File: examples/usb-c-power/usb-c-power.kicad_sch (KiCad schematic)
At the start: 10 parts, among them J1 USB4105-GF-A, J2 Fused 5 V OUT

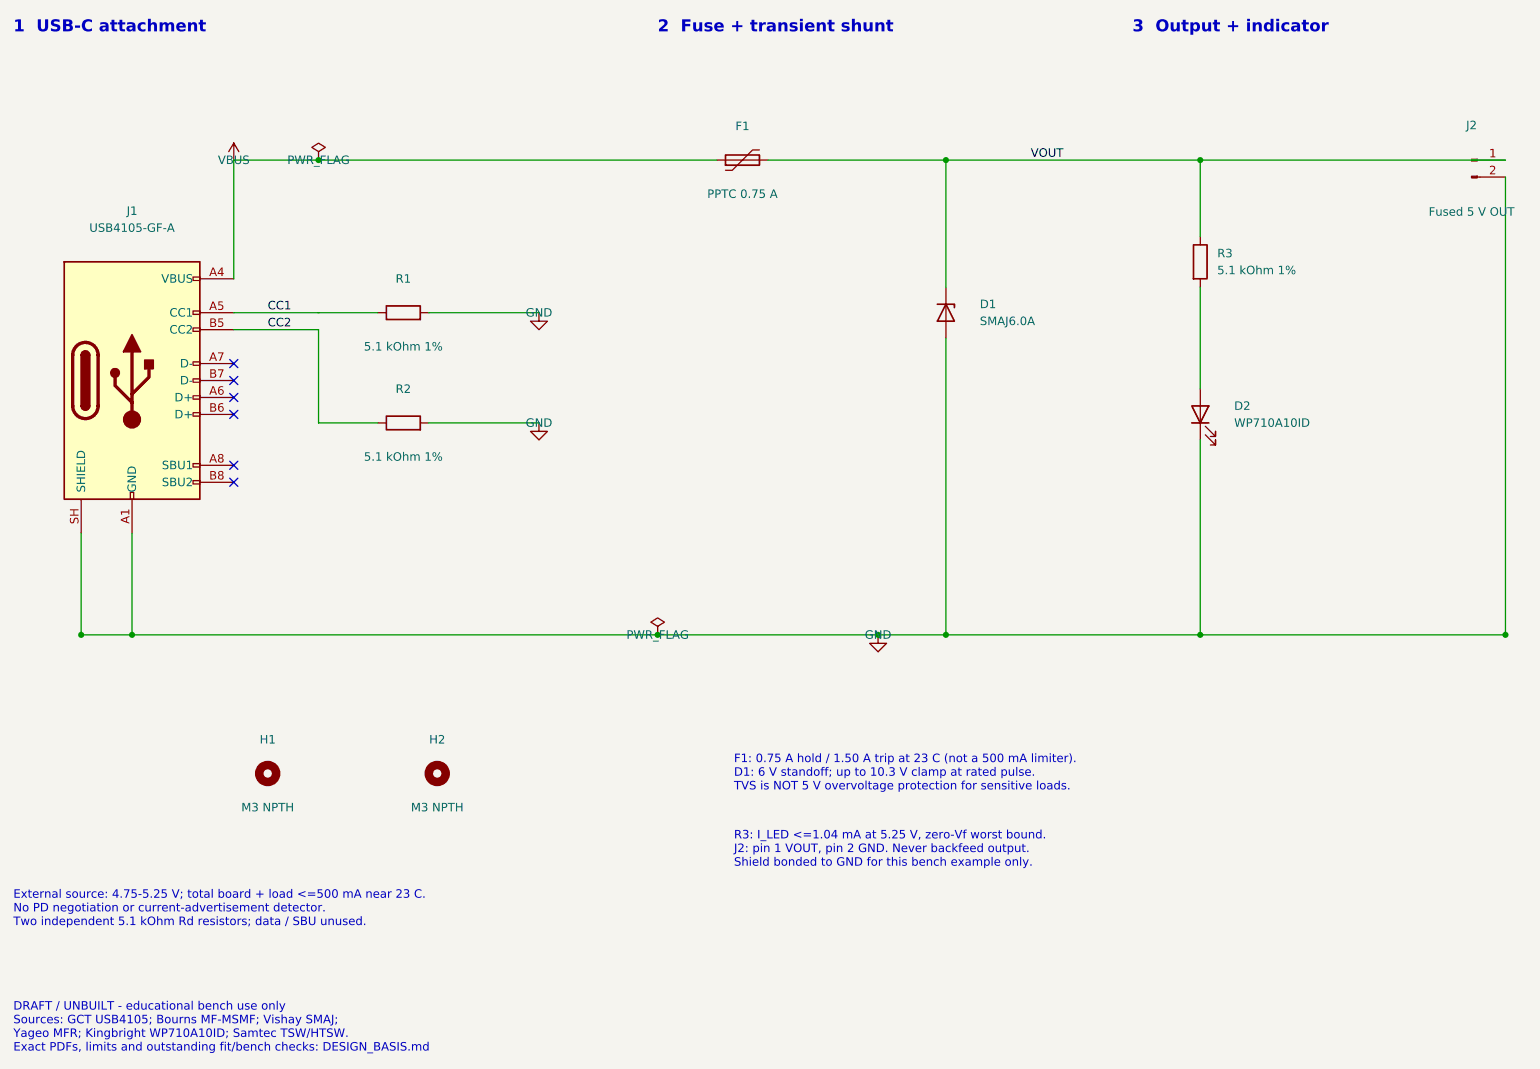
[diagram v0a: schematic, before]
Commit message: Resolve USB-C connector DRC with compatible manufacturer geometry
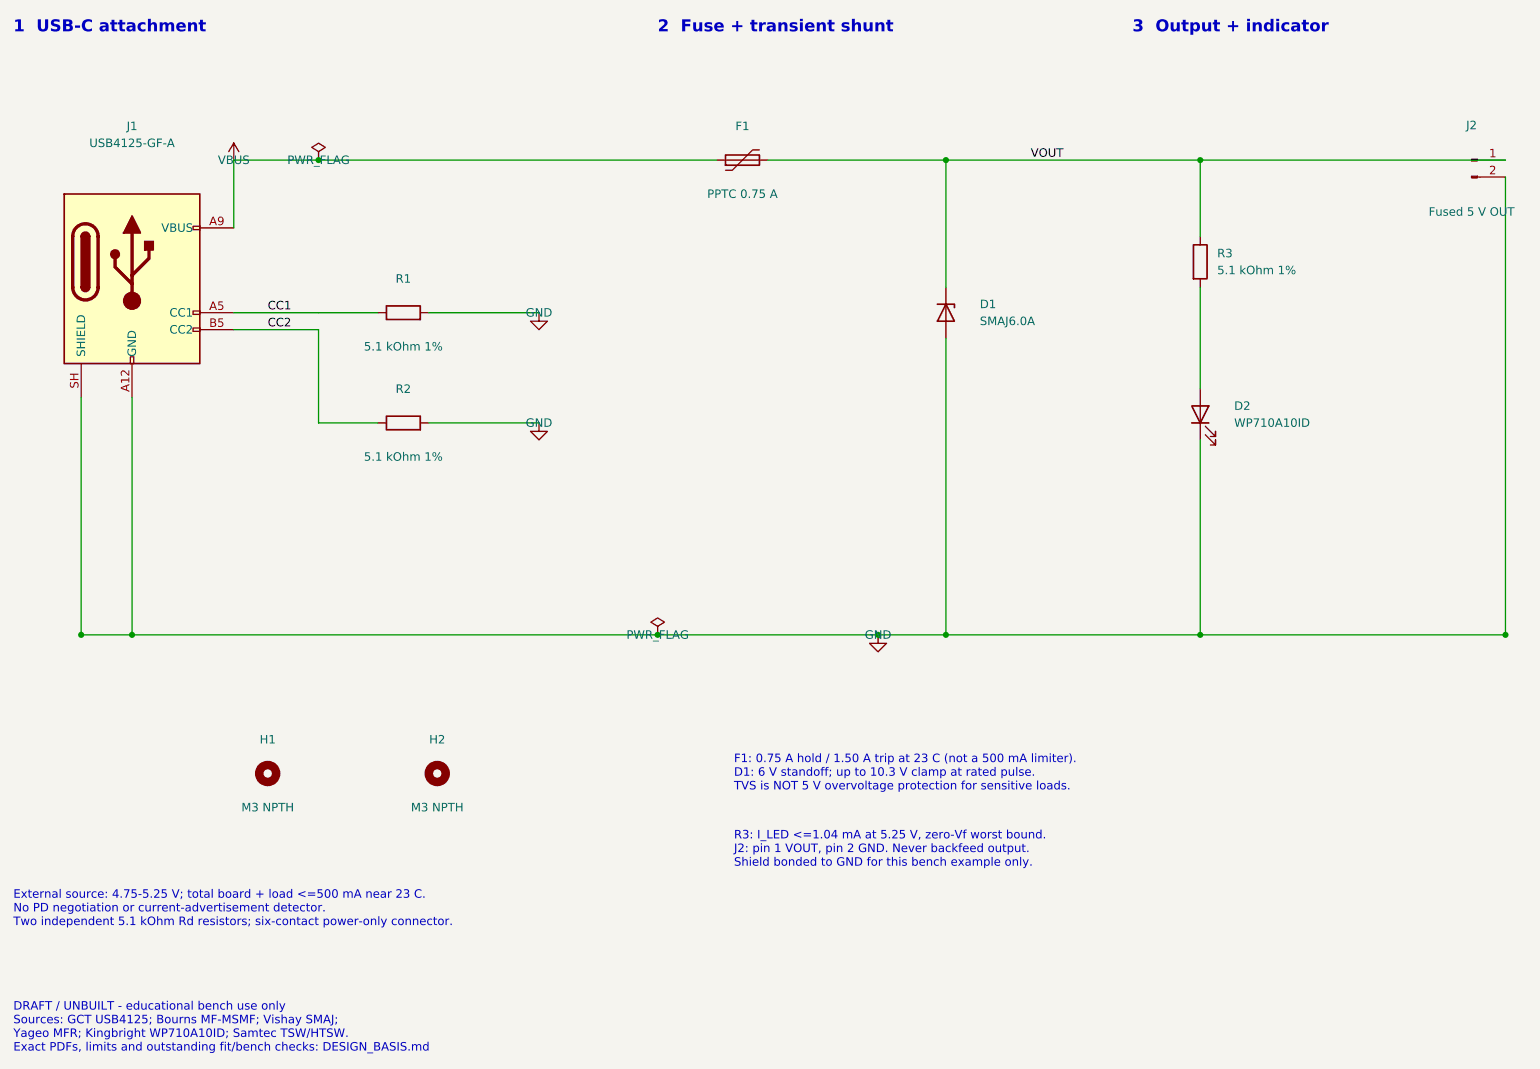
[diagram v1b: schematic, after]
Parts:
- J1: value USB4105-GF-A -> USB4125-GF-A; footprint USBC:USB_C_Receptacle_GCT_USB4105-xx-A_16P_TopMnt_Horizontal -> USBC:USB_C_Receptacle_GCT_USB4125-xx-x_6P_TopMnt_Horizontal; symbol USBC:USB_C_Receptacle_USB2.0_16P -> USBC:USB_C_Receptacle_PowerOnly_6P; MPN USB4105-GF-A -> USB4125-GF-A
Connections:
- net GND: no longer J1.A1 (GND), J1.B1 (GND)
- net VBUS: no longer J1.A4 (VBUS), J1.B4 (VBUS)
- no-connect marks 6 -> 0
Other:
- note added: "DRAFT / UNBUILT - educational bench use only Sources: GCT USB4125; Bourns MF-MSMF; Vishay SMAJ; Yageo MFR; Kingbright WP710A10ID; Samtec TSW/HTSW. Exact PDFs, limits and outstanding fit/bench checks: DESIGN_BASIS.md"
- note added: "External source: 4.75-5.25 V; total board + load <=500 mA near 23 C. No PD negotiation or current-advertisement detector. Two independent 5.1 kOhm Rd resistors; six-contact power-only connector."
- note removed: "DRAFT / UNBUILT - educational bench use only Sources: GCT USB4105; Bourns MF-MSMF; Vishay SMAJ; Yageo MFR; Kingbright WP710A10ID; Samtec TSW/HTSW. Exact PDFs, limits and outstanding fit/bench checks: DESIGN_BASIS.md"
- note removed: "External source: 4.75-5.25 V; total board + load <=500 mA near 23 C. No PD negotiation or current-advertisement detector. Two independent 5.1 kOhm Rd resistors; data / SBU unused."
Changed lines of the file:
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@@
 		(title "USB-C 5 V bench power entry")
 		(date "2026-10-29")
-		(rev "A")
+		(rev "B")
 		(company "PCB Copilot examples")
 		(comment 1 "DRAFT - unbuilt; externally qualified source and load required")
@@
 	(embedded_fonts no)
 	(symbol
-		(lib_id "USBC:USB_C_Receptacle_USB2.0_16P")
-		(at 40.64 87.63 0)
+		(lib_id "USBC:USB_C_Receptacle_PowerOnly_6P")
+		(at 40.64 72.39 0)
 		(unit 1)
 		(exclude_from_sim no)
@@
 		(dnp no)
 		(property "Reference" "J1"
-			(at 40.64 62.23 0)
-			(effects
-				(font
-					(size 1.27 1.27)
-				)
-			)
-		)
-		(property "Value" "USB4105-GF-A"
-			(at 40.64 64.77 0)
-			(effects
-				(font
-					(size 1.27 1.27)
-				)
-			)
-		)
-		(property "Footprint" "USBC:USB_C_Receptacle_GCT_USB4105-xx-A_16P_TopMnt_Horizontal"
+			(at 40.64 49.53 0)
+			(effects
+				(font
+					(size 1.27 1.27)
+				)
+			)
+		)
+		(property "Value" "USB4125-GF-A"
+			(at 40.64 52.07 0)
+			(effects
+				(font
+					(size 1.27 1.27)
+				)
+			)
+		)
+		(property "Footprint" "USBC:USB_C_Receptacle_GCT_USB4125-xx-x_6P_TopMnt_Horizontal"
 			(at 40.64 88.08 0)
 			(effects
@@
 			)
 		)
-		(property "Datasheet" "~"
+		(property "Datasheet" "https://gct.co/files/drawings/usb4125.pdf"
 			(at 40.64 88.08 0)
 			(effects
@@
 			)
 		)
-		(property "Description" ""
+		(property "Description" "Six-contact USB-C power-only receptacle; no data/SBU contacts"
 			(at 40.64 88.08 0)
 			(effects
@@
 				(hide yes)
 			)
-		)
-		(pin "A1"
-		)
-		(pin "A4"
-		)
-		(pin "A5"
-		)
-		(pin "A6"
-		)
-		(pin "A7"
-		)
-		(pin "A8"
-		)
-		(pin "A9"
-		)
-		(pin "A12"
-		)
-		(pin "B1"
-		)
-		(pin "B4"
-		)
-		(pin "B5"
-		)
-		(pin "B6"
-		)
-		(pin "B7"
-		)
-		(pin "B8"
-		)
-		(pin "B9"
-		)
-		(pin "B12"
-		)
-		(pin "SH"
 		)
 		(instances
@@
 			)
 		)
-		(property "MPN" "USB4105-GF-A"
+		(property "MPN" "USB4125-GF-A"
 			(at 40.64 88.08 0)
 			(effects
@@
 				(hide yes)
 			)
+		)
+		(pin "A5"
+		)
+		(pin "A9"
+		)
+		(pin "A12"
+		)
+		(pin "B5"
+		)
+		(pin "B9"
+		)
+		(pin "B12"
+		)
+		(pin "SH"
 		)
 	)
@@
 	(wire
 		(pts
-			(xy 55.88 72.39)
+			(xy 55.88 64.77)
 			(xy 55.88 54.61)
 		)
@@
 	(wire
 		(pts
-			(xy 40.64 110.49)
+			(xy 40.64 90.17)
 			(xy 40.64 125.73)
 		)
@@
 	(wire
 		(pts
-			(xy 33.02 110.49)
+			(xy 33.02 90.17)
 			(xy 33.02 125.73)
 		)
@@
 		(color 0 0 0 0)
 	)
-	(no_connect
-		(at 55.88 90.17)
-	)
-	(no_connect
-		(at 55.88 102.87)
-	)
-	(no_connect
-		(at 55.88 87.63)
-	)
-	(no_connect
-		(at 55.88 92.71)
-	)
-	(no_connect
-		(at 55.88 85.09)
-	)
-	(no_connect
-		(at 55.88 100.33)
-	)
 	(text "1  USB-C attachment"
 		(at 22.86 34.74 0)
@@
 		)
 	)
-	(text "External source: 4.75-5.25 V; total board + load <=500 mA near 23 C.\nNo PD negotiation or current-advertisement detector.\nTwo independent 5.1 kOhm Rd resistors; data / SBU unused."
+	(text "External source: 4.75-5.25 V; total board + load <=500 mA near 23 C.\nNo PD negotiation or current-advertisement detector.\nTwo independent 5.1 kOhm Rd resistors; six-contact power-only connector."
 		(at 22.86 166.82 0)
 		(effects
@@
 		)
 	)
-	(text "DRAFT / UNBUILT - educational bench use only\nSources: GCT USB4105; Bourns MF-MSMF; Vishay SMAJ;\nYageo MFR; Kingbright WP710A10ID; Samtec TSW/HTSW.\nExact PDFs, limits and outstanding fit/bench checks: DESIGN_BASIS.md"
+	(text "DRAFT / UNBUILT - educational bench use only\nSources: GCT USB4125; Bourns MF-MSMF; Vishay SMAJ;\nYageo MFR; Kingbright WP710A10ID; Samtec TSW/HTSW.\nExact PDFs, limits and outstanding fit/bench checks: DESIGN_BASIS.md"
 		(at 22.86 184.6 0)
 		(effects
